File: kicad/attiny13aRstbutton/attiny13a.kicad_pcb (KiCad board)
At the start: 2 copper layers, 28.3 x 21.3 mm, 8 parts, among them P1 CONN_01X04, P2 CONN_01X04, P3 CONN_01X06, SW1 SWITCH, U1 ATTINY13A-SSU

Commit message: Add capacitor across switch
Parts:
- added C2: C, Capacitors_SMD:C_0805_HandSoldering, F.Cu at (136.3, 99.6)
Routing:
- net /rst: track 59.1 -> 62.2 mm
- net Net-(C2-Pad1): track 12.1 -> 14.7 mm
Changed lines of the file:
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@@
 (kicad_pcb (version 20160815) (host pcbnew "(2017-01-24 revision 0b6147e)-makepkg")
   (general
-    (links 21)
+    (links 23)
     (no_connects 0)
     (area 119.558999 83.490999 148.030001 104.977001)
     (thickness 1.6)
     (drawings 24)
-    (tracks 45)
+    (tracks 49)
     (zones 0)
-    (modules 8)
+    (modules 9)
     (nets 10)
   )
@@
   (net 7 /pb3)
   (net 8 /pb4)
-  (net 9 "Net-(R1-Pad2)")
+  (net 9 "Net-(C2-Pad1)")
   (net_class Default "This is the default net class."
     (clearance 0.2)
@@
     (add_net /pb4)
     (add_net /rst)
-    (add_net "Net-(R1-Pad2)")
+    (add_net "Net-(C2-Pad1)")
   )
   (net_class power ""
@@
     (fp_line (start -1 0.625) (end -1 -0.625) (layer F.Fab) (width 0.1))
     (pad 2 smd rect (at 1.35 0 90) (size 1.5 1.3) (layers F.Cu F.Paste F.Mask)
-      (net 9 "Net-(R1-Pad2)"))
+      (net 9 "Net-(C2-Pad1)"))
     (pad 1 smd rect (at -1.35 0 90) (size 1.5 1.3) (layers F.Cu F.Paste F.Mask)
       (net 1 GND))
@@
       (net 6 /rst))
     (pad 1 thru_hole circle (at -3.81 -2.54) (size 1.397 1.397) (drill 0.8128) (layers *.Cu *.Mask)
-      (net 9 "Net-(R1-Pad2)"))
+      (net 9 "Net-(C2-Pad1)"))
     (pad 2 thru_hole circle (at 3.81 2.54) (size 1.397 1.397) (drill 0.8128) (layers *.Cu *.Mask)
       (net 6 /rst))
     (pad 1 thru_hole circle (at 3.81 -2.54) (size 1.397 1.397) (drill 0.8128) (layers *.Cu *.Mask)
-      (net 9 "Net-(R1-Pad2)"))
+      (net 9 "Net-(C2-Pad1)"))
+  )
+  (module Capacitors_SMD:C_0805_HandSoldering (layer F.Cu)
+    (at 136.271 99.568 270)
+    (descr "Capacitor SMD 0805, hand soldering")
+    (tags "capacitor 0805")
+    (attr smd)
+    (fp_text reference C2 (at 0 -2.1 270) (layer F.SilkS)
+      (effects (font (size 1 1) (thickness 0.15)))
+    )
+    (fp_text value C (at 0 2.1 270) (layer F.Fab)
+      (effects (font (size 1 1) (thickness 0.15)))
+    )
+    (fp_line (start -0.5 0.85) (end 0.5 0.85) (layer F.SilkS) (width 0.12))
+    (fp_line (start 0.5 -0.85) (end -0.5 -0.85) (layer F.SilkS) (width 0.12))
+    (fp_line (start 2.3 -1) (end 2.3 1) (layer F.CrtYd) (width 0.05))
+    (fp_line (start -2.3 -1) (end -2.3 1) (layer F.CrtYd) (width 0.05))
+    (fp_line (start -2.3 1) (end 2.3 1) (layer F.CrtYd) (width 0.05))
+    (fp_line (start -2.3 -1) (end 2.3 -1) (layer F.CrtYd) (width 0.05))
+    (fp_line (start -1 -0.625) (end 1 -0.625) (layer F.Fab) (width 0.1))
+    (fp_line (start 1 -0.625) (end 1 0.625) (layer F.Fab) (width 0.1))
+    (fp_line (start 1 0.625) (end -1 0.625) (layer F.Fab) (width 0.1))
+    (fp_line (start -1 0.625) (end -1 -0.625) (layer F.Fab) (width 0.1))
+    (pad 2 smd rect (at 1.25 0 270) (size 1.5 1.25) (layers F.Cu F.Paste F.Mask)
+      (net 6 /rst))
+    (pad 1 smd rect (at -1.25 0 270) (size 1.5 1.25) (layers F.Cu F.Paste F.Mask)
+      (net 9 "Net-(C2-Pad1)"))
+    (model Capacitors_SMD.3dshapes/C_0805_HandSoldering.wrl
+      (at (xyz 0 0 0))
+      (scale (xyz 1 1 1))
+      (rotate (xyz 0 0 0))
+    )
   )
   (gr_line (start 147.955 83.566) (end 147.828 83.566) (angle 90) (layer Edge.Cuts) (width 0.15))
@@
   (segment (start 138.811 91.694) (end 133.883643 91.694) (width 0.25) (layer F.Cu) (net 5))
   (segment (start 133.883643 91.694) (end 133.798143 91.6085) (width 0.25) (layer F.Cu) (net 5))
+  (segment (start 133.985 102.616) (end 134.473 102.616) (width 0.25) (layer F.Cu) (net 6) (status C00000))
+  (segment (start 134.473 102.616) (end 136.271 100.818) (width 0.25) (layer F.Cu) (net 6) (status C00000))
   (segment (start 145.288 91.313) (end 141.986 94.615) (width 0.25) (layer B.Cu) (net 6))
   (segment (start 141.986 102.616) (end 133.985 102.616) (width 0.25) (layer B.Cu) (net 6))
@@
   (segment (start 123.317 94.234) (end 124.6725 92.8785) (width 0.25) (layer F.Cu) (net 8))
   (segment (start 124.6725 92.8785) (end 128.398143 92.8785) (width 0.25) (layer F.Cu) (net 8))
+  (segment (start 133.985 97.536) (end 135.489 97.536) (width 0.25) (layer F.Cu) (net 9) (status 400000))
+  (segment (start 135.489 97.536) (end 136.271 98.318) (width 0.25) (layer F.Cu) (net 9) (status 800000))
   (segment (start 126.365 97.536) (end 125.523 97.536) (width 0.25) (layer F.Cu) (net 9))
   (segment (start 125.523 97.536) (end 122.936 100.123) (width 0.25) (layer F.Cu) (net 9))

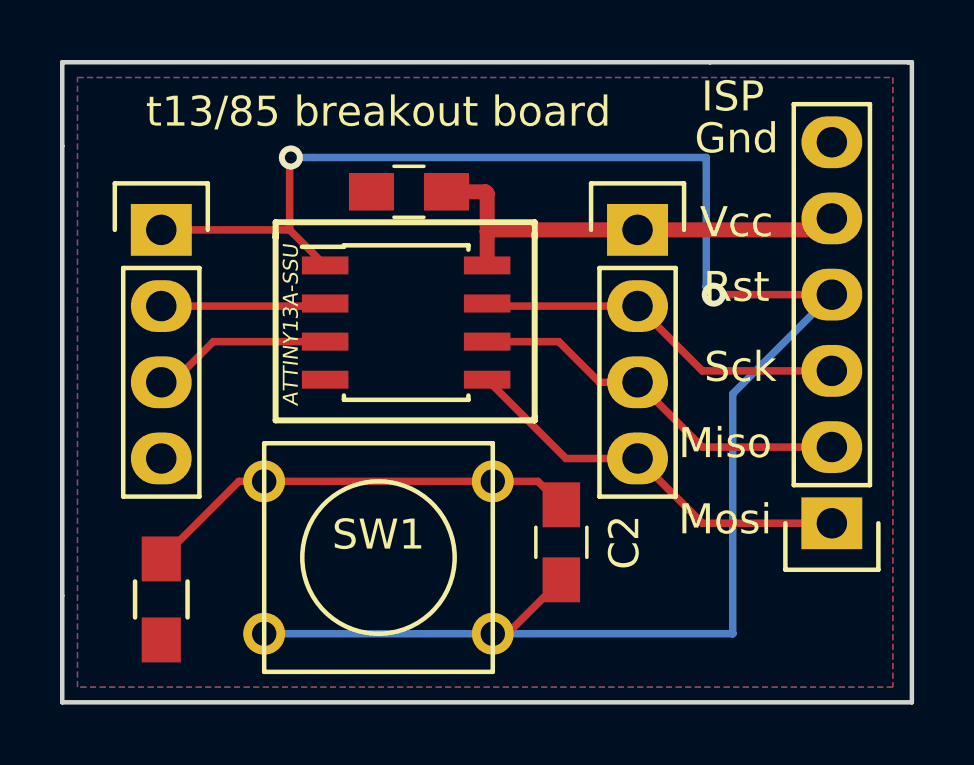
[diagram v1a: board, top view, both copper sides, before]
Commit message: Add 6mm switch button
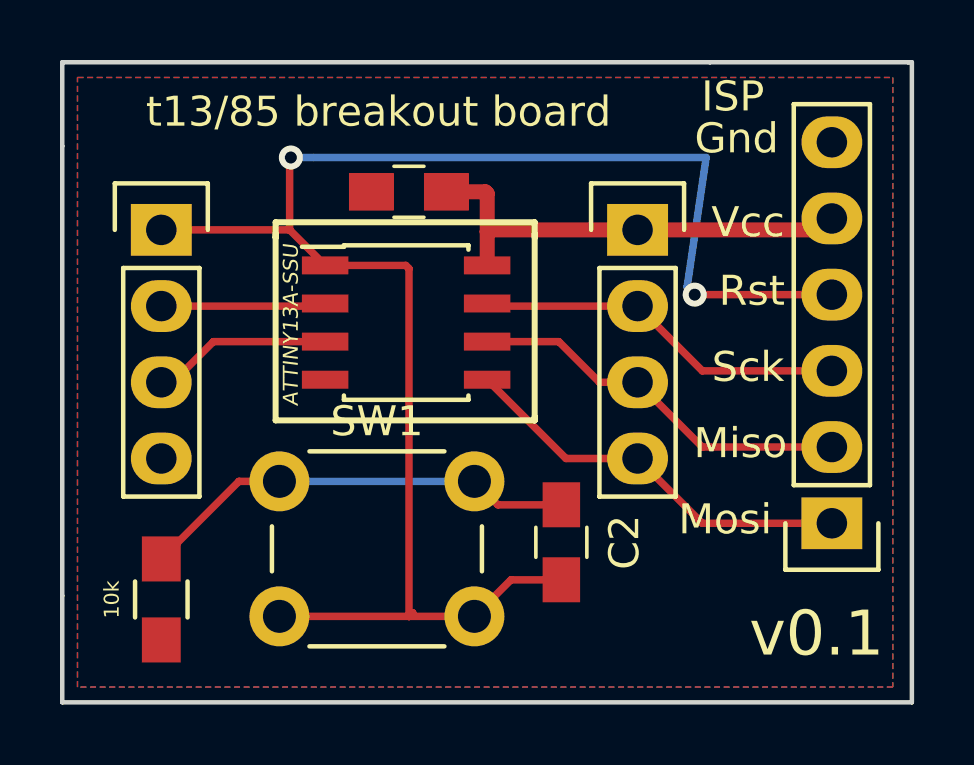
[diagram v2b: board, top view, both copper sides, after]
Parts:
- SW1: footprint Buttons_Switches_ThroughHole:SW_PUSH_SMALL -> Buttons_Switches_ThroughHole:SW_PUSH_6mm
- moved SW1 4.17 mm to (126.9, 97.5)
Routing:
- net /rst: track 62.2 -> 56.6 mm
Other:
- board text added: "v0.1"

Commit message: Add attiny13a
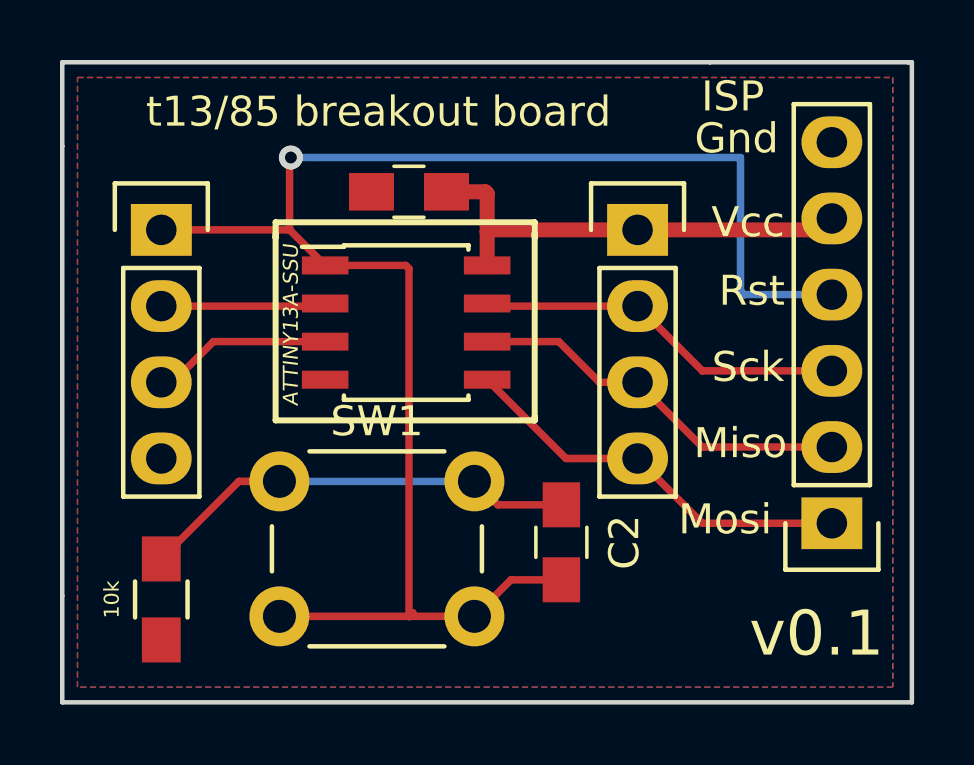
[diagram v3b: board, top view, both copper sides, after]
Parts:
- moved G*** 4.50 mm to (130.9, 92.3)
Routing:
- net /rst: track 56.6 -> 56.0 mm, vias 2 -> 1
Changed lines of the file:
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@@
   )
   (module led2layer:superme (layer B.Cu)
-    (at 129.286 96.52 180)
+    (at 130.937 92.329 180)
     (fp_text reference G*** (at 0 0 180) (layer B.SilkS) hide
       (effects (font (thickness 0.3)) (justify mirror))
     )
-    (fp_text value "made by ami 2017" (at -6.985 2.54 270) (layer B.SilkS)
+    (fp_text value "made by ami 2017" (at -5.3975 -1.651 270) (layer B.SilkS)
       (effects (font (size 0.8 0.8) (thickness 0.2)) (justify mirror))
     )
@@
   (segment (start 138.811 91.694) (end 133.883643 91.694) (width 0.25) (layer F.Cu) (net 5))
   (segment (start 133.883643 91.694) (end 133.798143 91.6085) (width 0.25) (layer F.Cu) (net 5))
+  (segment (start 145.288 91.313) (end 142.367 91.313) (width 0.25) (layer B.Cu) (net 6) (status 400000))
+  (segment (start 127.213643 86.781357) (end 127.213643 89.154) (width 0.25) (layer F.Cu) (net 6))
+  (segment (start 127.254 86.741) (end 127.213643 86.781357) (width 0.25) (layer F.Cu) (net 6))
+  (via (at 127.254 86.741) (size 0.8) (drill 0.4) (layers F.Cu B.Cu) (net 6))
+  (segment (start 128.016 86.741) (end 127.254 86.741) (width 0.25) (layer B.Cu) (net 6))
+  (segment (start 141.097 86.741) (end 128.016 86.741) (width 0.25) (layer B.Cu) (net 6))
+  (segment (start 142.24 86.741) (end 141.097 86.741) (width 0.25) (layer B.Cu) (net 6))
+  (segment (start 142.24 91.186) (end 142.24 86.741) (width 0.25) (layer B.Cu) (net 6))
+  (segment (start 142.367 91.313) (end 142.24 91.186) (width 0.25) (layer B.Cu) (net 6))
   (segment (start 126.873 102.036) (end 131.1995 102.036) (width 0.25) (layer F.Cu) (net 6))
   (segment (start 131.1995 102.036) (end 131.318 101.9175) (width 0.25) (layer F.Cu) (net 6))
@@
   (segment (start 136.271 100.818) (end 134.591 100.818) (width 0.25) (layer F.Cu) (net 6))
   (segment (start 134.591 100.818) (end 133.373 102.036) (width 0.25) (layer F.Cu) (net 6))
-  (segment (start 145.288 91.313) (end 140.716 91.313) (width 0.25) (layer F.Cu) (net 6))
-  (segment (start 127.213643 86.781357) (end 127.213643 89.154) (width 0.25) (layer F.Cu) (net 6))
-  (segment (start 127.254 86.741) (end 127.213643 86.781357) (width 0.25) (layer F.Cu) (net 6))
-  (via (at 127.254 86.741) (size 0.8) (drill 0.4) (layers F.Cu B.Cu) (net 6))
-  (segment (start 128.016 86.741) (end 127.254 86.741) (width 0.25) (layer B.Cu) (net 6))
-  (segment (start 141.097 86.741) (end 128.016 86.741) (width 0.25) (layer B.Cu) (net 6))
-  (segment (start 140.462 91.059) (end 141.097 86.741) (width 0.25) (layer B.Cu) (net 6))
-  (segment (start 140.716 91.313) (end 140.462 91.059) (width 0.25) (layer B.Cu) (net 6))
-  (via (at 140.716 91.313) (size 0.8) (drill 0.4) (layers F.Cu B.Cu) (net 6))
   (segment (start 122.936 89.154) (end 127.213643 89.154) (width 0.25) (layer F.Cu) (net 6))
   (segment (start 127.213643 89.154) (end 128.398143 90.3385) (width 0.25) (layer F.Cu) (net 6))
